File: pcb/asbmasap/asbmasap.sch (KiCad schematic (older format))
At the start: 17 parts

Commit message: feat(pbc): add clock control
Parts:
- removed D?: D, symbol Device:D
- removed Q?: Q_NMOS_DGS, symbol Device:Q_NMOS_DGS
- removed Q? (x2): Q_PMOS_DSG, symbol Device:Q_PMOS_DSG
- added C?: 4.7uF, symbol Device:C_Small
- added C?: 1uF, symbol Device:C_Small
- added C?: 22uF, symbol Device:C_Small
- added C? (x4): 12pF, symbol Device:C
- added D?: D_Schottky_Small, symbol Device:D_Schottky_Small
- added L?: L_Small, symbol Device:L_Small
- added Q?: Q_PMOS_DGS, symbol Device:Q_PMOS_DGS
- added R?: 2M, symbol Device:R_Small
- added R?: 180K, symbol Device:R_Small
- added U?: TPS61200DRC, Package_SON:Texas_S-PVSON-N10_ThermalVias, symbol Regulator_Switching:TPS61200DRC
- added U?: nRF52840, Package_DFN_QFN:Nordic_AQFN-73-1EP_7x7mm_P0.5mm, symbol MCU_Nordic:nRF52840
- added Y? (x2): 32MHz, symbol Device:Crystal
- R?: value R -> 10K
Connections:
- net labels added: 5v_OUT, XC1, XC2, XL1, XL2
- wire segments 50 -> 117
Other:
- note added: "BATTERY CHARGER"
- note added: "Clock control"
- note added: "Load sharing circuit"
- note added: "Optional"
- note added: "Voltage regulation"
- moved on the sheet: C?, R?

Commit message: feat(pcb): annotate components and rearrange
Update asbmasap.sch
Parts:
- added AE1: Antenna, symbol Device:Antenna
- added C10, C13, C14, C22, C23: 100nF, symbol Device:C_Small
- added C11, C17, C20: 1uF, symbol Device:C_Small
- added C12, C15, C16, C19: 4.7uF, symbol Device:C_Small
- added C18: 47nF, symbol Device:C_Small
- added C21: 100pF, symbol Device:C_Small
- added C24: 1.5pF, symbol Device:C_Small
- added C25: 0.5pF, symbol Device:C_Small
- added C26: 0.8pF, symbol Device:C_Small
- added L2, L5: 10uH, symbol Device:L_Small
- added L3: 15nH, symbol Device:L_Small
- added L4: 4.7nH, symbol Device:L_Small
- added R9: 10k, symbol Device:R_Small
- added SW1: SW_Push, symbol Switch:SW_Push
- Y1: renamed from Y?; value 32MHz -> 32.768kHz
- gave numbers to parts that had none: 26
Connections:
- net labels added: ANT, DCC, DEC1, DEC3, DEC4, DEC5, DEC6, DECUSB, RESET, VBUS, VDDH, VDD_nRF, VSS_PA, VVD_nRF
- wire segments 117 -> 198
- no-connect marks 4 -> 5
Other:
- note added: "Antenna"
- note added: "Cl = 12.5pF"
- note added: "Cl = 12pF"
- note added: "Decoupling Capacitors"
- note added: "Reset"
- note removed: "Optional"
- moved on the sheet: C6, C7, C8, C9, U3, Y1, Y2

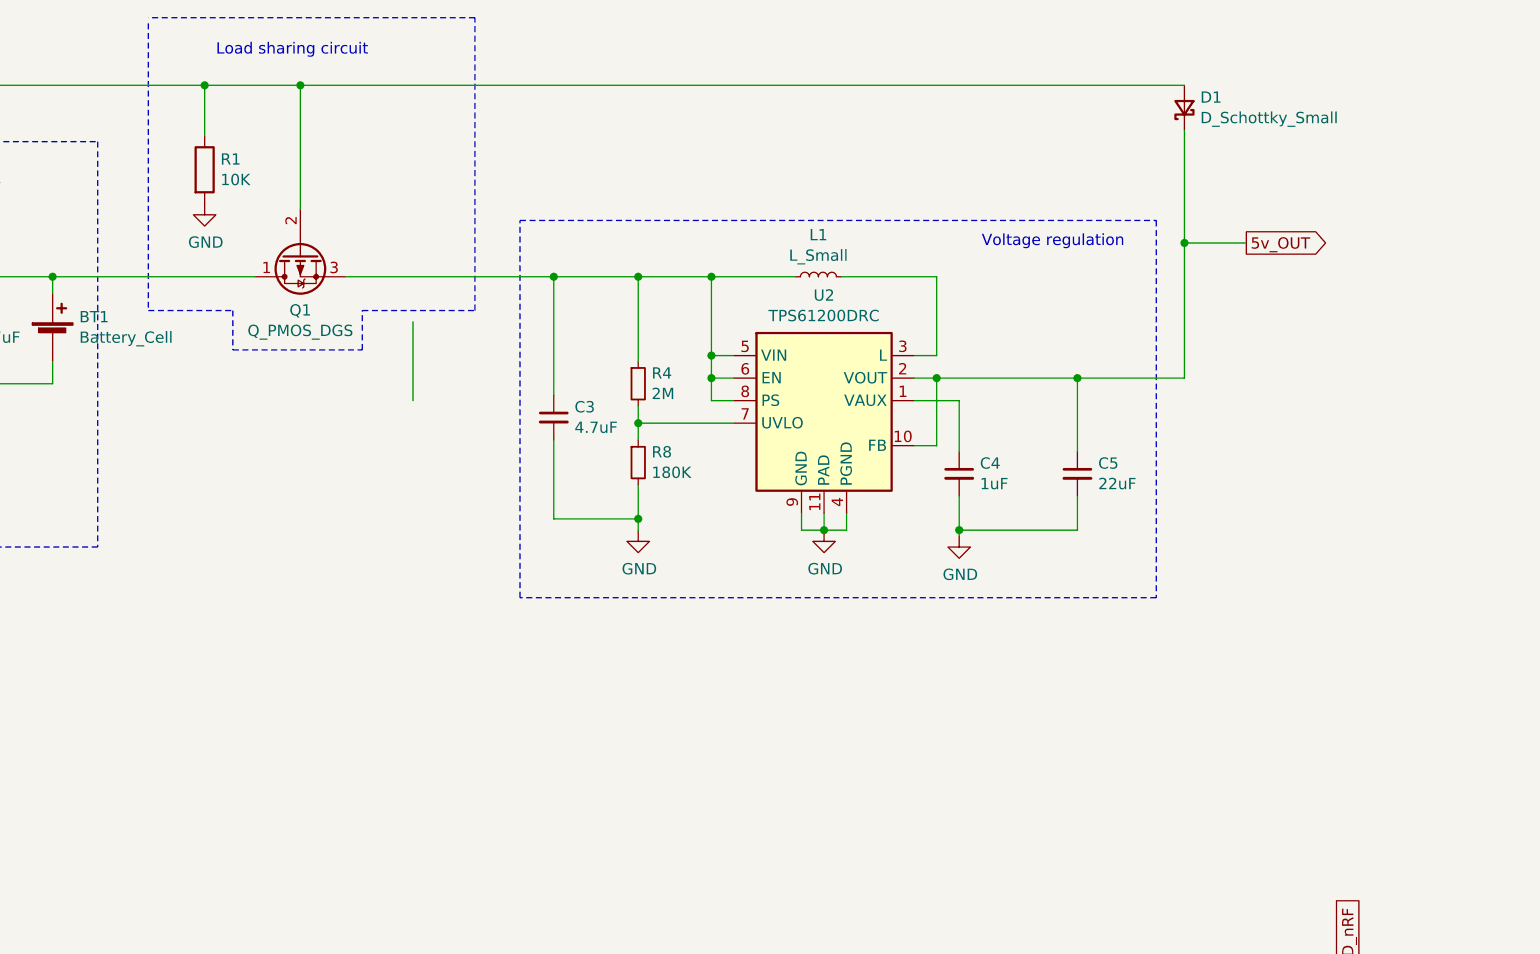
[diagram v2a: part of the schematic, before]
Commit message: refactor(pcb): refactor load sharing and voltage regulation circuit
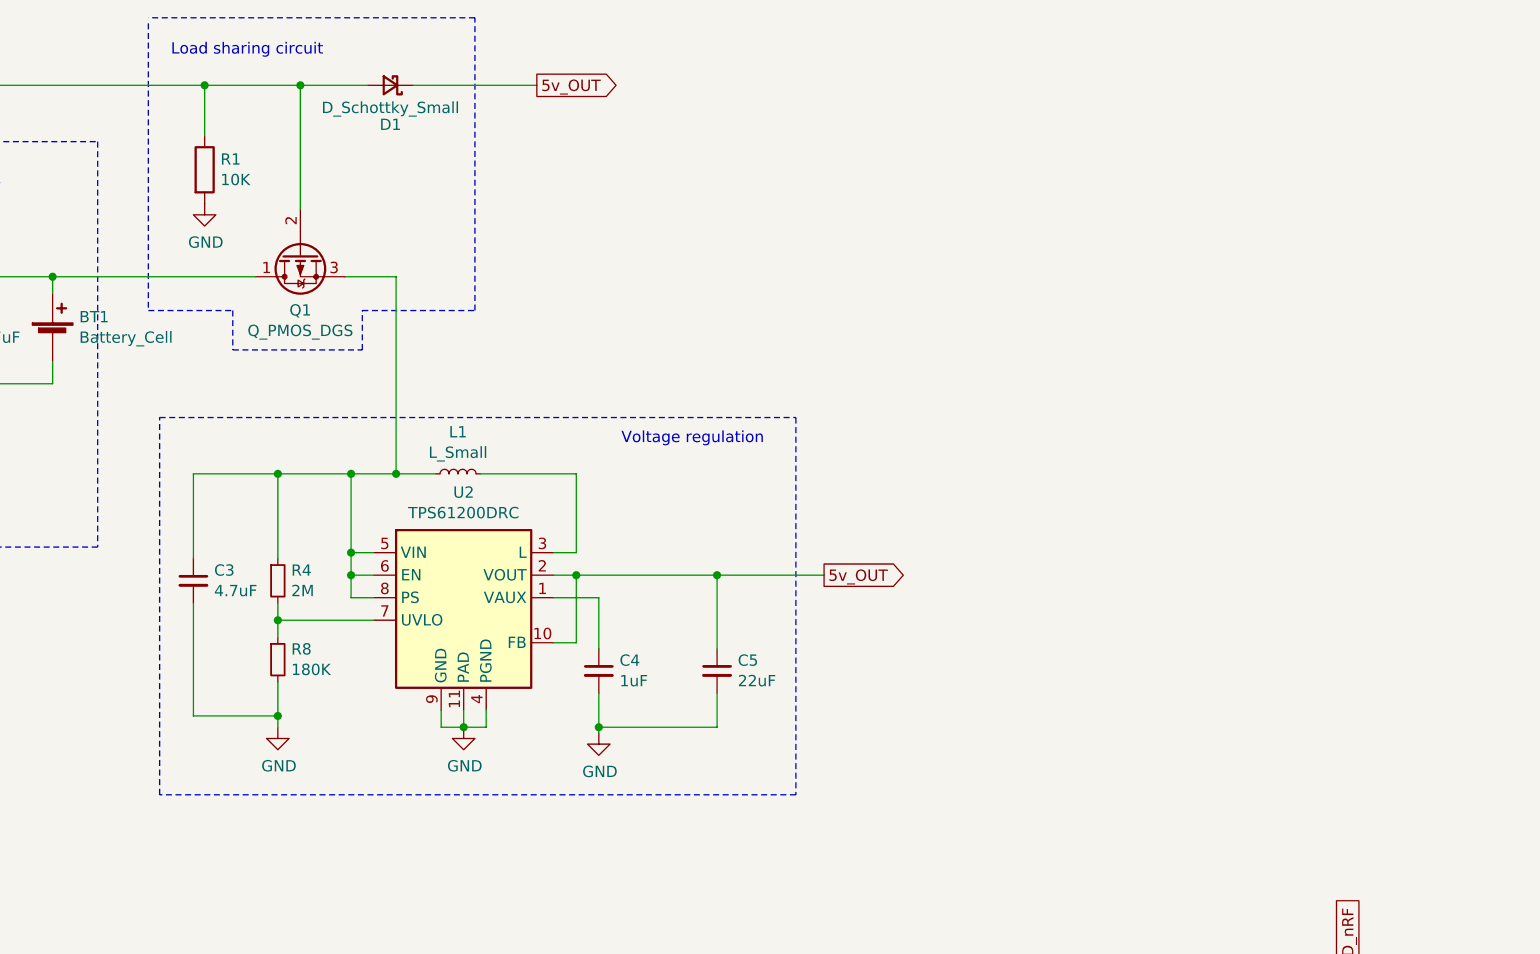
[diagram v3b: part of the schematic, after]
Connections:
- wire segments 198 -> 197
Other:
- moved on the sheet: C3, C4, C5, D1, L1, R4, R8, U2
